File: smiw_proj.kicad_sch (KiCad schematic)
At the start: 25 parts, among them J3 Conn_01x02, J4 Conn_01x02, J7 Conn_02x05, J8 Conn_02x05, J9 Conn_01x02, SW1 SW_Push, U1 LM2596S-5, U2 M5 Stamp-S3, U3 LD1117S33TR_SOT223

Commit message: Add files via upload
Jeszcze PCB
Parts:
- removed D8: D_Schottky, symbol Device:D_Schottky
- removed J7, J8: Conn_02x05, symbol Connector_Generic:Conn_02x05_Counter_Clockwise
- removed J9: Conn_01x02, symbol Connector_Generic:Conn_01x02
- added D3: SS14, symbol Device:D_Schottky
- added J1: Conn_02x06_Odd_Even, symbol Connector_Generic:Conn_02x06_Odd_Even
- added J2: Conn_02x05_Odd_Even, symbol Connector_Generic:Conn_02x05_Odd_Even
- C1, C7: renamed from 100u/16V1; value C1 -> 100uF/16V
- C2: value 100n -> 100nF
- C3: renamed from C4; value 220u/6V3 -> 220uF/6V3
- C4: renamed from C3; value 220n -> 220nF
- C5: renamed from 10u/16V1; value C6 -> 10uF/16V
- C6: renamed from 100n2; value C5 -> 100nF
- C8: renamed from C6; value 100n -> 100nF
- D2: renamed from D9; value D_Schottky -> SS14
- L1: renamed from 10uH1; value L -> 10uH
- L2: renamed from L1; value 33u -> 33uH
- renumbered R7 to R1, R14 to R2
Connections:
- net 12V: now also D3.1 (K), J1.1 (Pin_1)
- net CPU_GND: now also J1.9 (Pin_9)
- net DRIVER IN1: now also J1.2 (Pin_2)
- net DRIVER IN2: now also J1.4 (Pin_4)
- net DRIVER IN3: now also J1.8 (Pin_8)
- net DRIVER IN4: now also J1.10 (Pin_10)
- net ENC A: now also J1.11 (Pin_11)
- net ENC B: now also J1.12 (Pin_12)
- net GND: now also J1.7 (Pin_7), J2.3 (Pin_3), J2.5 (Pin_5), J2.7 (Pin_7), J2.9 (Pin_9)
- net MISO: now also J2.4 (Pin_4)
- net MOSI: now also J2.2 (Pin_2)
- net PWM A: now also J1.6 (Pin_6)
- net SCK: now also J2.6 (Pin_6)
- net VDD: now also J2.1 (Pin_1)
- net at J4.2 (Pin_2), R2.2: now also D3.2 (A)
- net 5V renamed Vcc
- net Vcc: now also J1.3 (Pin_3)
- net FRAM CS renamed #FRAM CS
- net #FRAM CS: now also J2.10 (Pin_10)
- net SD CS renamed #SD CS
- net #SD CS: now also J2.8 (Pin_8)
- net VDD SD renamed Vdd
- net Vdd: now also J1.5 (Pin_5)
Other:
- note removed: "Zasilanie"
- moved on the sheet: C5, C6, L3, U3

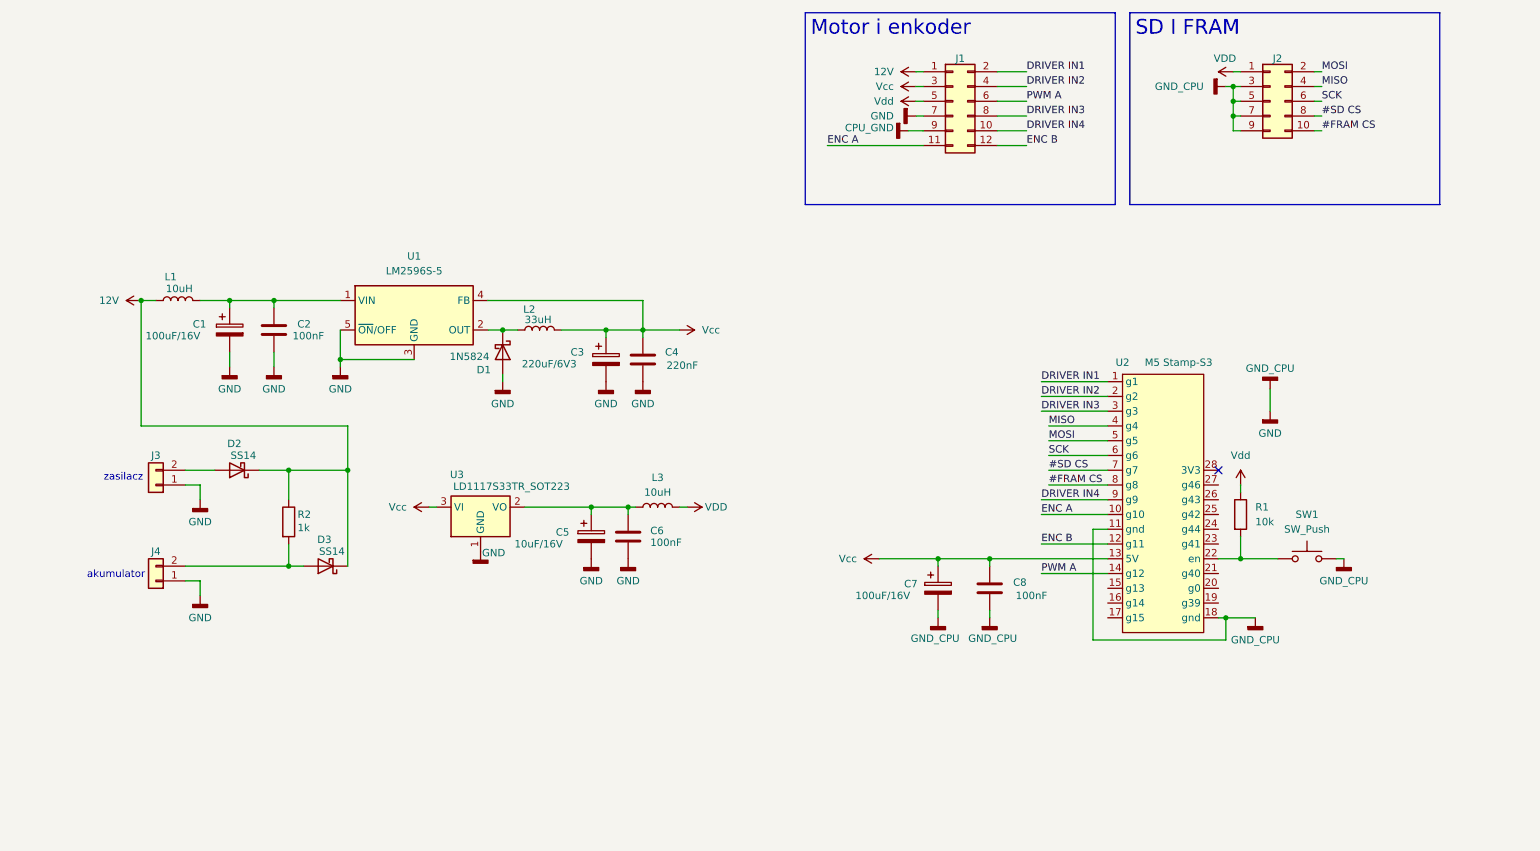
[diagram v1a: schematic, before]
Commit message: poprawki po 'pracy' michala na schemacie. Poprawione PCB pamieci po Kubie. Grubsze sciezki, poprawiona pozycja decoupling capacitora
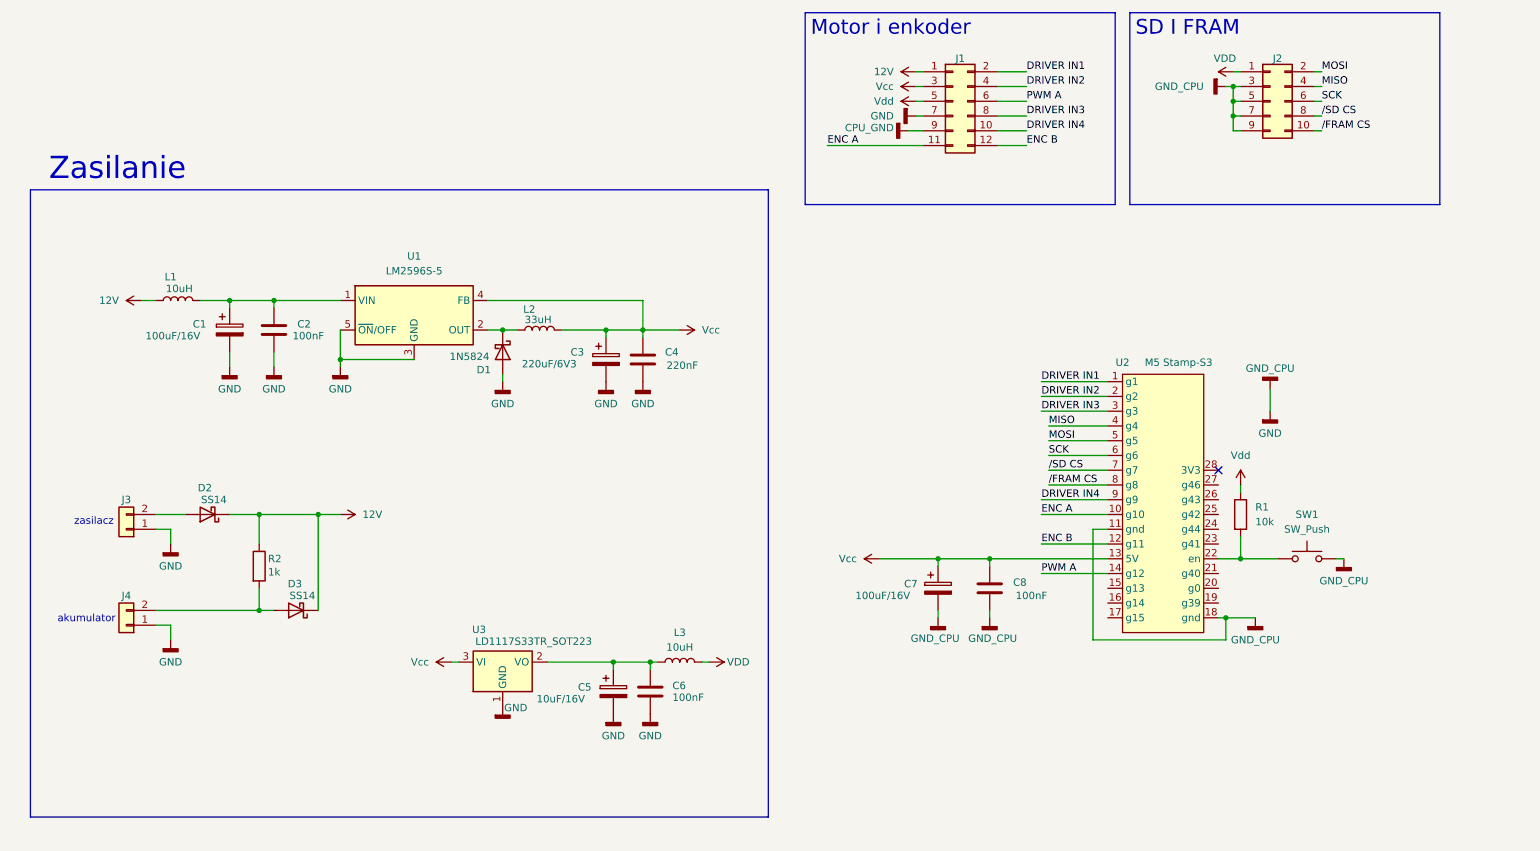
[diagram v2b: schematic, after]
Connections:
- net #FRAM CS renamed /FRAM CS
- net #SD CS renamed /SD CS
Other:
- note added: "Zasilanie"
- moved on the sheet: C5, C6, D2, D3, J3, J4, L3, R2, U3

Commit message: dodane footprinty
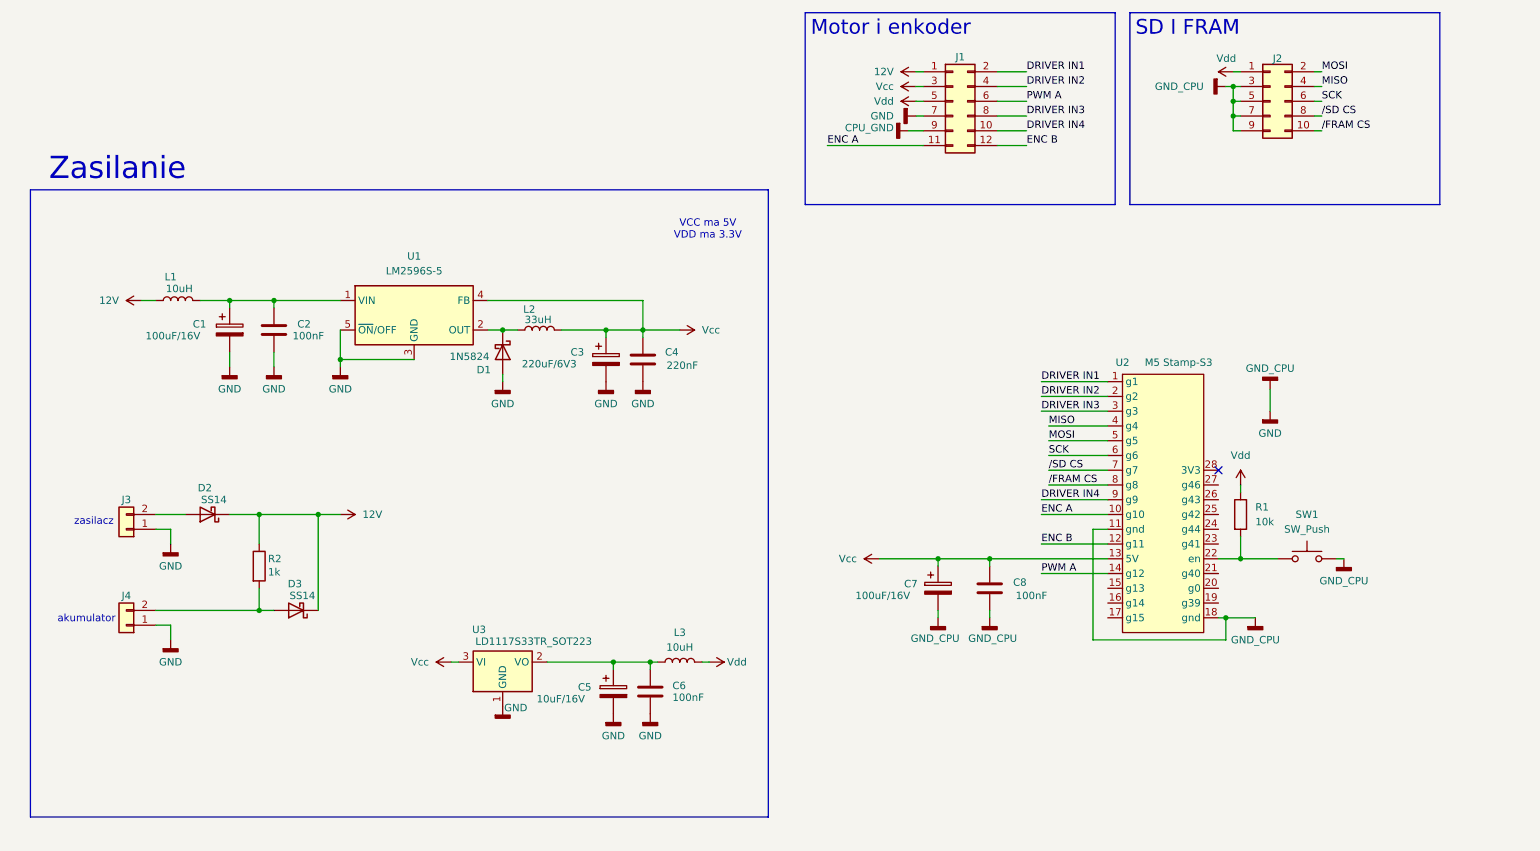
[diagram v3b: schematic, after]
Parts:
- C1, C3, C4, C7: footprint (none) -> Capacitor_THT:CP_Axial_L10.0mm_D4.5mm_P15.00mm_Horizontal
- C2, C6, C8: footprint (none) -> Capacitor_SMD:C_0805_2012Metric
- C5: footprint (none) -> Capacitor_THT:CP_Radial_D5.0mm_P2.50mm
- D2, D3: footprint (none) -> Diode_SMD:D_SMA
- J1: footprint (none) -> Connector_PinSocket_1.00mm:PinSocket_2x06_P1.00mm_Vertical_SMD
- J2: footprint (none) -> Connector_PinSocket_1.00mm:PinSocket_2x05_P1.00mm_Vertical_SMD
- J3, J4: footprint (none) -> Connector_PinSocket_1.00mm:PinSocket_1x02_P1.00mm_Vertical_SMD_Pin1Left
- L1, L2, L3: footprint (none) -> Inductor_SMD:L_0805_2012Metric
- R1, R2: footprint (none) -> Resistor_SMD:R_0805_2012Metric
- SW1: footprint (none) -> Button_Switch_THT:SW_PUSH_6mm
- U2: footprint stamps3254:Stamp-S3_PIN2.54_DIP -> Library:M5Stamp-S3
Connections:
- net VDD is gone; now on net Vdd: J2.1 (Pin_1), L3.2
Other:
- note added: "VCC ma 5V VDD ma 3.3V"

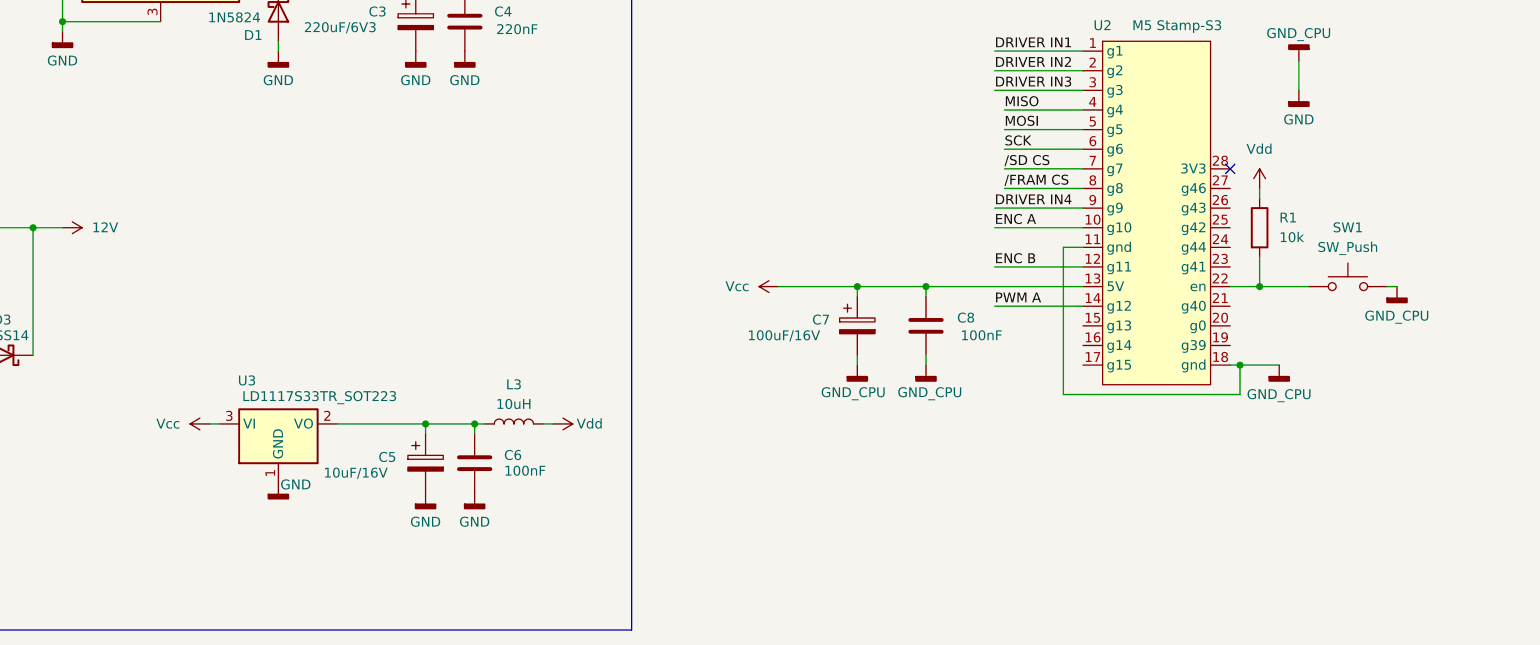
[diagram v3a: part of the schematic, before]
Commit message: pcb prawie gotowe. czekam na werdykt o Vcc
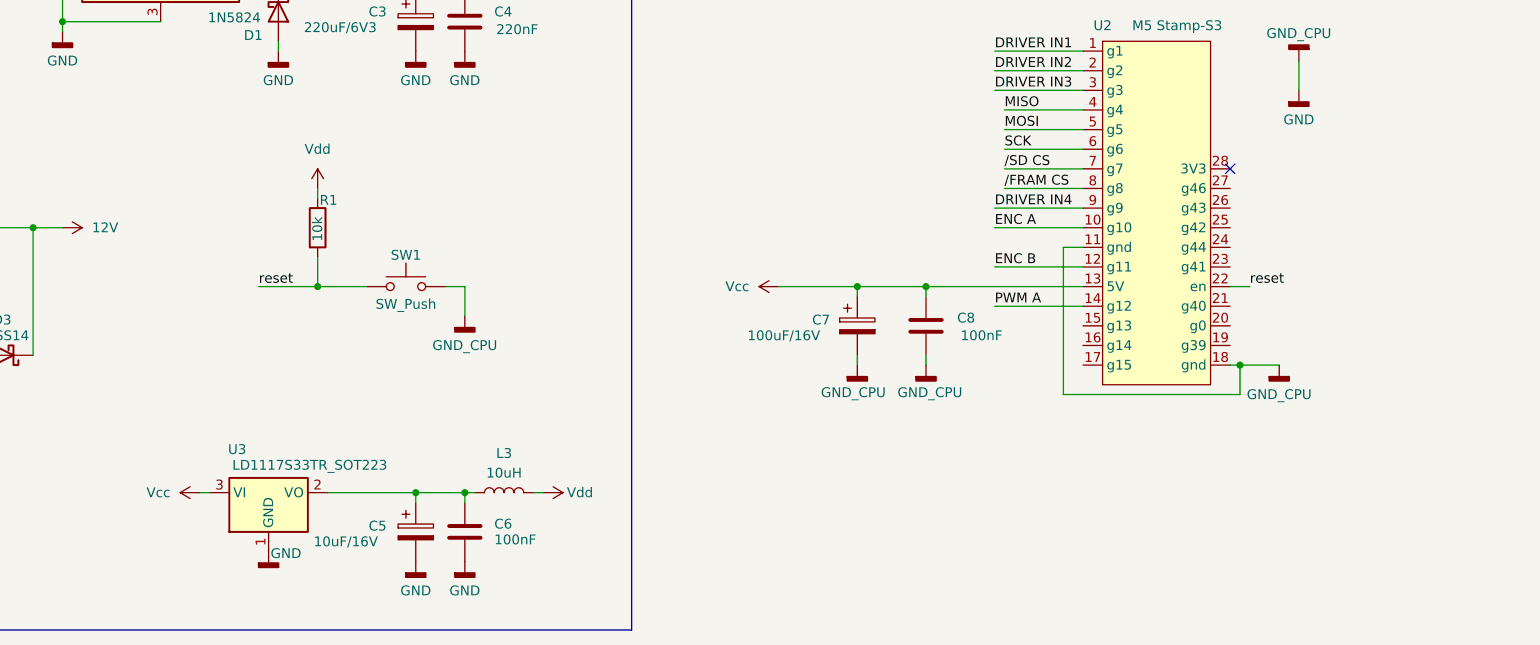
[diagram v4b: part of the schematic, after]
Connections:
- net reset: now reaches R1.2, SW1.1, U2.22 (en)
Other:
- moved on the sheet: C5, C6, L3, U3

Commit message: Add files via upload
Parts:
- C1, C3, C7: footprint Capacitor_THT:CP_Axial_L10.0mm_D4.5mm_P15.00mm_Horizontal -> Capacitor_SMD:C_Elec_6.3x7.7
- C2, C6, C8: footprint Capacitor_SMD:C_0805_2012Metric -> Capacitor_SMD:C_0805_2012Metric_Pad1.18x1.45mm_HandSolder
- C4: footprint Capacitor_THT:CP_Axial_L10.0mm_D4.5mm_P15.00mm_Horizontal -> Capacitor_SMD:C_0805_2012Metric_Pad1.18x1.45mm_HandSolder
- C5: footprint Capacitor_THT:CP_Radial_D5.0mm_P2.50mm -> Capacitor_SMD:C_Elec_6.3x7.7
- D1: footprint Diode_THT:D_DO-201AD_P15.24mm_Horizontal -> Diode_SMD:D_SMC
- D2: footprint Diode_SMD:D_SMA -> Diode_SMD:D_SMC
- J1: footprint Connector_PinSocket_1.00mm:PinSocket_2x06_P1.00mm_Vertical_SMD -> Connector_PinHeader_2.54mm:PinHeader_2x06_P2.54mm_Vertical_SMD
- J2: footprint Connector_PinSocket_1.00mm:PinSocket_2x05_P1.00mm_Vertical_SMD -> Connector_PinHeader_2.54mm:PinHeader_2x05_P2.54mm_Vertical_SMD
- J3, J4: footprint Connector_PinSocket_1.00mm:PinSocket_1x02_P1.00mm_Vertical_SMD_Pin1Left -> Connector_PinHeader_2.54mm:PinHeader_1x02_P2.54mm_Vertical_SMD_Pin1Left
- L1, L2, L3: footprint Inductor_SMD:L_0805_2012Metric -> Inductor_SMD:L_Bourns_SRR1260
- R1, R2: footprint Resistor_SMD:R_0805_2012Metric -> Resistor_SMD:R_1206_3216Metric_Pad1.30x1.75mm_HandSolder
- SW1: footprint Button_Switch_THT:SW_PUSH_6mm -> Button_Switch_SMD:SW_SPST_PTS647_Sx50
- U2: footprint Library:M5Stamp-S3 -> M5_Stamp:Stamp-S3_PIN1.27_Socket
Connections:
- net Vdd: no longer J2.1 (Pin_1), L3.2
- net reset: no longer names the net of R1.2, SW1.1, U2.22 (en)
- net /FRAM CS renamed #FRAM CS
- net /SD CS renamed #SD CS
- new net VDD: J2.1 (Pin_1), L3.2
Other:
- note removed: "VCC ma 5V VDD ma 3.3V"
- note removed: "Zasilanie"
- moved on the sheet: C5, C6, D2, D3, J3, J4, L3, R2, U3

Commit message: poprawka
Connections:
- net #FRAM CS renamed /FRAM CS
- net #SD CS renamed /SD CS
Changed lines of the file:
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@@
+		)
+	)
+	(text_box "Zasilanie\n\n"
+		(exclude_from_sim no)
+		(at 30.48 54.61 0)
+		(size 120.65 72.39)
+		(margins 0.9525 0.9525 0.9525 0.9525)
+		(stroke
+			(width 0)
+			(type solid)
+		)
+		(fill
+			(type none)
+		)
+		(effects
+			(font
+				(size 2.54 2.54)
+			)
+			(justify left top)
 		)
 	)
@@
 		)
 	)
-	(label "#FRAM CS"
+	(label "{slash}FRAM CS"
 		(at 248.92 38.1 0)
 		(effects
@@
 		)
 	)
-	(label "#SD CS"
+	(label "{slash}SD CS"
 		(at 201.93 96.52 0)
 		(effects
@@
 		)
 	)
-	(label "#FRAM CS"
+	(label "{slash}FRAM CS"
 		(at 201.93 99.06 0)
 		(effects
@@
 		)
 	)
-	(label "#SD CS"
+	(label "{slash}SD CS"
 		(at 248.92 35.56 0)
 		(effects

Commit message: już prawie, jedno sprawdzenie
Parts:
- C1, C3, C5, C7: footprint Capacitor_SMD:C_Elec_6.3x7.7 -> Capacitor_SMD:CP_Elec_6.3x5.3; KiLib_Generator (none) -> capacitor/THT/other
- C2, C6, C8, L1, L2, L3, R1, R2: KiLib_Generator (none) -> SMD_2terminal_chip_molded
- C4: KiLib_Generator (none) -> capacitor/THT/other
- D1: KiLib_Generator (none) -> diode/THT
- J1: footprint Connector_PinHeader_2.54mm:PinHeader_2x06_P2.54mm_Vertical_SMD -> Connector_PinSocket_1.00mm:PinSocket_2x05_P1.00mm_Vertical_SMD; KiLib_Generator (none) -> connector/pin_header_socket
- J2: footprint Connector_PinHeader_2.54mm:PinHeader_2x05_P2.54mm_Vertical_SMD -> Connector_PinSocket_1.00mm:PinSocket_2x05_P1.00mm_Vertical_SMD; KiLib_Generator (none) -> connector/pin_header_socket
- J3, J4: footprint Connector_PinHeader_2.54mm:PinHeader_1x02_P2.54mm_Vertical_SMD_Pin1Left -> Connector_PinSocket_1.00mm:PinSocket_1x02_P1.00mm_Vertical_SMD_Pin1Left; KiLib_Generator (none) -> connector/pin_header_socket
- U1: KiLib_Generator (none) -> package/TO_SOT/SMD
- U2: footprint M5_Stamp:Stamp-S3_PIN1.27_Socket -> Library2:Stamp-S3_PIN1.27_Socket
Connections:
- net VDD is gone; now on net Vdd: J2.1 (Pin_1), L3.2
- net reset: now reaches R1.2, SW1.1, U2.22 (en)
- net /FRAM CS renamed ~{FRAM CS}
- net /SD CS renamed ~{SD CS}
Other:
- note added: "VCC ma 5V VDD ma 3.3V"
- note added: "Zasilanie"
- moved on the sheet: C5, C6, D2, D3, J3, J4, L3, R2, U3
